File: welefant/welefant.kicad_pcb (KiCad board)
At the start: 2 copper layers, 80 x 90 mm, 72 parts, among them J1 Conn_02x11_Odd_Even, J2 Conn_02x11_Odd_Even, Q1 AO3400A, Q2 AO3401A, Q3 AO3401A, Q4 AO3400A, SW1 TS-1187A-B-A-B, SW2 TS-1187A-B-A-B, U1 ESP32-S3-WROOM-1-N8, U2 welefant, U3 XB8089D, U4 TP4056, U5 HE9073A33M5R, U6 MT3608L, U7 SK6812MINI-E_C5149201, U8 SK6812MINI-E_C5149201

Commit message: blubb
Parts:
- removed BUZZER1: MLT-8530, easyeda2kicad:BUZ-SMD_4P-L8.5-W8.5-P8.50-TL
- removed D5, D6, D7: SS34, easyeda2kicad:SMA_L4.3-W2.6-LS5.2-RD
- removed D8: BAV99,215, easyeda2kicad:SOT-23-3_L2.9-W1.6-P1.90-LS2.8-BR
- removed LED22, LED23, LED24, LED25: SK6812MINI-E, hacrafu:SK6812MINI-E-handsolder
- removed MIC1: ZTS6117, easyeda2kicad:MIC-SMD_4P-L2.8-W1.9-P1.84-TL_ZTS6117
- removed Q4: AO3400A, easyeda2kicad:SOT-23-3_L2.9-W1.6-P1.90-LS2.8-BR
- added ANT1: ANTENNA, hacrafu:antenna, F.Cu at (71.3, 36.8)
- added BT1: Battery, hacrafu:LiPo_Recycled_welefant, F.Cu at (59.4, 114.0)
- added C12: 10u, easyeda2kicad:C0603, F.Cu at (66.0, 50.7)
- added C13: 1u, easyeda2kicad:C0603, F.Cu at (67.6, 50.7)
- added C14: 1u, easyeda2kicad:C0603, F.Cu at (71.4, 49.9)
- added C15: 100n, easyeda2kicad:C0603, F.Cu at (69.3, 50.7)
- added C16: 100n, easyeda2kicad:C0603, F.Cu at (67.0, 55.8)
- added C17: 100n, easyeda2kicad:C0603, F.Cu at (73.5, 50.7)
- added C18: 4p7, easyeda2kicad:C0402, F.Cu at (76.0, 51.8)
- added C19: 3p3, easyeda2kicad:C0402, F.Cu at (76.0, 47.6)
- added C20: 100n, easyeda2kicad:C0603, F.Cu at (68.3, 70.3)
- added C21: 100n, easyeda2kicad:C0603, F.Cu at (77.8, 54.0)
- added C22: 1u, easyeda2kicad:C0603, F.Cu at (66.7, 70.3)
- added C23: 100n, easyeda2kicad:C0603, F.Cu at (79.2, 54.0)
- added C24: 100n, easyeda2kicad:C0603, F.Cu at (60.3, 59.5)
- added C25: 1u, easyeda2kicad:C0603, F.Cu at (87.3, 107.1)
- added C8: 10u, easyeda2kicad:C0603, F.Cu at (58.2, 71.0)
- added CLED1: yellow, easyeda2kicad:LED0603-RD-YELLOW, F.Cu at (48.5, 77.7)
- added D4: 1N5819WS, Diode_SMD:D_SOD-323, F.Cu at (48.1, 79.8)
- added J3: Conn_02x6_Odd_Even, hacrafu:PinHeader_2x06_P2.54mm_Vertical_SMD_handsolder, F.Cu at (92.0, 50.3)
- added L2: 2n2, easyeda2kicad:L0603, F.Cu at (75.4, 49.7)
- added LEDH_L1: SK6812MINI-E, hacrafu:SK6812MINI-E-handsolder, F.Cu at (80.0, 66.0)
- added LEDH_R1: SK6812MINI-E, hacrafu:SK6812MINI-E-handsolder, F.Cu at (63.2, 66.0)
- added R11: 10K, easyeda2kicad:R0603, F.Cu at (50.5, 88.1)
- added R12: 330, easyeda2kicad:R0603, F.Cu at (48.5, 76.1)
- added R13: 10K, easyeda2kicad:R0603, F.Cu at (48.9, 68.6)
- added R14: 1K, easyeda2kicad:R0603, F.Cu at (50.4, 68.6)
- added R15: 390K, easyeda2kicad:R0603, F.Cu at (56.5, 67.5)
- added R16: 100K, easyeda2kicad:R0603, F.Cu at (56.5, 69.4)
- added R17: 3K3, easyeda2kicad:R0603_NEW, F.Cu at (59.4, 76.2)
- added R18: 0, easyeda2kicad:R0603, F.Cu at (82.1, 59.3)
- added R19: 10K, easyeda2kicad:R0603, F.Cu at (44.2, 47.4)
- added R20: 330, easyeda2kicad:R0603, F.Cu at (66.8, 59.8)
- added R21: 0, easyeda2kicad:R0603, F.Cu at (75.3, 63.5)
- added R22: 0, easyeda2kicad:R0603, F.Cu at (74.0, 63.5)
- added R23: 0, easyeda2kicad:R0603, F.Cu at (72.5, 63.5)
- added R24: 0, easyeda2kicad:R0603, F.Cu at (71.2, 63.5)
- added R25: 0, easyeda2kicad:R0603, F.Cu at (69.8, 63.5)
- added SW3: BOOT, easyeda2kicad:SW-SMD_4P-L5.1-W5.1-P3.70-LS6.5-TL-2, F.Cu at (105.0, 45.5)
- added SW4: GPIO33, easyeda2kicad:SW-SMD_4P-L5.1-W5.1-P3.70-LS6.5-TL-2, F.Cu at (38.5, 52.5)
- added SW5: IO34, easyeda2kicad:SW-SMD_4P-L5.1-W5.1-P3.70-LS6.5-TL-2, F.Cu at (105.0, 52.5)
- added X1: 40 MHz, easyeda2kicad:OSC-SMD_4P-L3.2-W2.5-BL_SIT8008BI, F.Cu at (79.7, 59.0)
- C1: value 0.1u -> 33n; footprint easyeda2kicad:C0402_NEW -> easyeda2kicad:C0603
- C10: value 10u -> 15p
- C11: value 0.1u -> 15p; footprint easyeda2kicad:C0402_NEW -> easyeda2kicad:C0603
- C2: value 10u -> 33n
- C6: value 22u -> 1u; footprint easyeda2kicad:C0805 -> easyeda2kicad:C0603
- C7: value 22u -> 10u; footprint easyeda2kicad:C0805 -> easyeda2kicad:C0603
- C9: value 0.1u -> 10u; footprint easyeda2kicad:C0402_NEW -> easyeda2kicad:C0603
- D1: value 5V6 -> 3V3
- D3: value 3V3 -> 5V6
- J1: value Conn_02x11_Odd_Even -> Conn_01x02; footprint Connector_PinHeader_2.54mm:PinHeader_2x11_P2.54mm_Vertical_SMD -> Connector_JST:JST_PH_B2B-PH-K_1x02_P2.00mm_Vertical
- J2: value Conn_02x11_Odd_Even -> Conn_02x7_Odd_Even; footprint Connector_PinHeader_2.54mm:PinHeader_2x11_P2.54mm_Vertical_SMD -> hacrafu:PinHeader_2x07_P2.54mm_Vertical_SMD_handsolder
- L1: value 10u -> 2n2; footprint easyeda2kicad:IND-SMD_L8.0-W8.0 -> easyeda2kicad:L0603
- LED21: value SK6812MINI-E -> blue; footprint hacrafu:SK6812MINI-E-handsolder -> easyeda2kicad:LED0603-FD_BLUE
- Q1: value AO3400A -> AO3401A; footprint easyeda2kicad:SOT-23-3_L2.9-W1.6-P1.90-LS2.8-BR -> easyeda2kicad:SOT-23_L2.9-W1.3-P1.90-LS2.4-BR
- R1: value 5.1K -> 10K
- R10: value 10K -> 1K
- R2: value 1K -> 5.1K
- R3: value 5.1K -> 1K
- R4, R5: value 2.4K -> 270
- R6: value 10K -> 150
- R7: value 110K -> 150
- R8: value 110K -> 5.1K
- R9: value 15K -> 100K
- SW1: value TS-1187A-B-A-B -> ON-OFF; footprint easyeda2kicad:SW-SMD_4P-L5.1-W5.1-P3.70-LS6.5-TL-2 -> easyeda2kicad:SW-TH_K3-1296S-E1
- SW2: value TS-1187A-B-A-B -> RESET
- U1: value ESP32-S3-WROOM-1-N8 -> RT9080-33GJ5; footprint easyeda2kicad:WIFIM-SMD_ESP32-S3-WROOM-1-N8 -> easyeda2kicad:TSOT-23-5_L2.9-W1.6-P0.95-LS2.8-BL
- U2: value welefant -> Audio Jack PJ-324; footprint hacrafu:welefant -> easyeda2kicad:AUDIO-TH_PJ-32400
- U3: value XB8089D -> SD18OB261-060; footprint easyeda2kicad:SOIC-8_L5.0-W4.0-P1.27-LS6.0-BL-EP2.0 -> hacrafu:MIC-SMD_SD18OB261-060
- U5: value HE9073A33M5R -> welefant; footprint easyeda2kicad:SOT-23-5_L3.0-W1.7-P0.95-LS2.8-BL -> hacrafu:welefant; moved to B.Cu
- U6: value MT3608L -> 128MBit Flash; footprint easyeda2kicad:SOT-23-6_L2.9-W1.7-P0.95-LS2.8-BL -> easyeda2kicad:SOIC-8_L5.3-W5.3-P1.27-LS8.0-BL
- U7: value SK6812MINI-E_C5149201 -> ESP32-S3; footprint hacrafu:SK6812MINI-E-handsolder -> easyeda2kicad:QFN-56_L7.0-W7.0-P0.40-TL-EP4.0
- U8: value SK6812MINI-E_C5149201 -> Reset 2.8V; footprint hacrafu:SK6812MINI-E-handsolder -> easyeda2kicad:SOT-23-3_L2.9-W1.6-P1.90-LS2.8-BR
- moved J1 122.2 mm to (97.7, 103.2)
- moved LED13 115.2 mm to (87.2, 98.0), turned to 180 degrees
- moved LED17 107.7 mm to (87.2, 103.0), turned to 180 degrees
- moved LED15 105.3 mm to (67.2, 98.0), turned to 180 degrees
- moved LED16 104.6 mm to (57.2, 98.0), turned to 180 degrees
- moved LED14 102.7 mm to (77.2, 98.0), turned to 180 degrees
- moved LED18 101.7 mm to (77.2, 103.0), turned to 180 degrees
- moved SW1 96.5 mm to (42.8, 82.2), turned to 0 degrees
- moved U2 96.0 mm to (50.5, 111.2), turned to 6 degrees
- moved C5 94.2 mm to (46.2, 88.8), turned to -90 degrees
- moved LED9 93.8 mm to (87.2, 93.0), turned to 180 degrees
- moved LED19 92.5 mm to (67.2, 103.0), turned to 180 degrees
- moved LED11 92.1 mm to (67.2, 93.0), turned to 180 degrees
- moved LED10 89.0 mm to (77.2, 93.0), turned to 180 degrees
- moved LED2 88.9 mm to (77.2, 83.0), turned to 180 degrees
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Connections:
- C1 pad 1: Net-(C1-Pad1) -> GND
- C10 pad 1: Net-(BUZZER1-Pad1) -> /XTAL_N
- C10 pad 2: /GND -> GND
- C11 pad 1: Net-(R14-Pad2) -> GND
- C2 pad 1: /Power/VBAT -> GND
- C2 pad 2: /GND -> Net-(C2-Pad2)
- C3 pad 1: /Power/VUSB -> GND
- C3 pad 2: /GND -> /V33
- C4 pad 1: Net-(Q2-Pad2) -> Net-(C1-Pad2)
- C4 pad 2: /GND -> Net-(C4-Pad2)
- C5 pad 1: /GND -> Net-(C2-Pad2)
- C5 pad 2: /Power/V33 -> Net-(C5-Pad2)
- C6 pad 1: /Power/V5 -> GND
- C6 pad 2: /GND -> /VBUS
- C7 pad 1: Net-(C7-Pad1) -> /V5
- C7 pad 2: /GND -> GND
- C9 pad 1: /VEXT -> GND
- C9 pad 2: /GND -> /VBAT
- D1 pad 1: /Power/VUSB -> /USB_DP
- D1 pad 2: /GND -> GND
- D2 pad 1: /Power/USB_DP -> /USB_DN
- D2 pad 2: /GND -> GND
- D3 pad 1: /Power/USB_DN -> /V5
- D3 pad 2: /GND -> GND
- J1 pad 1: unconnected-(J1-Pad1) -> /VBAT
- J1 pad 2: unconnected-(J1-Pad2) -> GND
- J2 pad 1: unconnected-(J2-Pad1) -> GND
- J2 pad 10: unconnected-(J2-Pad10) -> /MIC_CLK
- J2 pad 11: unconnected-(J2-Pad11) -> /AUDIO_PWM_R
- J2 pad 12: unconnected-(J2-Pad12) -> /AUDIO_PWM_L
- J2 pad 13: unconnected-(J2-Pad13) -> /USB_DP
- J2 pad 14: unconnected-(J2-Pad14) -> /USB_DN
- J2 pad 2: unconnected-(J2-Pad2) -> /V33
- J2 pad 3: unconnected-(J2-Pad3) -> /RX
- J2 pad 4: unconnected-(J2-Pad4) -> /V5
- J2 pad 5: unconnected-(J2-Pad5) -> /TX
- J2 pad 6: unconnected-(J2-Pad6) -> /BAT_SENS
- J2 pad 7: unconnected-(J2-Pad7) -> /BAT_SENS_EN
- J2 pad 8: unconnected-(J2-Pad8) -> /MIC_DATA
- J2 pad 9: unconnected-(J2-Pad9) -> /JACK_SENS
- L1 pad 1: Net-(D7-Pad2) -> /V33
- L1 pad 2: Net-(C7-Pad1) -> Net-(C17-Pad2)
- LED1 pad 1: /LEDs/VUSB -> /VEXT
- LED1 pad 2: unconnected-(LED1-Pad2) -> Net-(LED1-DOUT)
- LED1 pad 3: /LEDs/GND -> GND
- LED1 pad 4: Net-(LED1-Pad4) -> /LED_MATRIX
- LED10 pad 1: /LEDs/VUSB -> /VEXT
- LED10 pad 2: Net-(LED10-Pad2) -> Net-(LED10-DOUT)
- LED10 pad 3: /LEDs/GND -> GND
- LED10 pad 4: unconnected-(LED10-Pad4) -> Net-(LED10-DIN)
- LED11 pad 1: /LEDs/VUSB -> /VEXT
- LED11 pad 2: unconnected-(LED11-Pad2) -> Net-(LED11-DOUT)
- LED11 pad 3: /LEDs/GND -> GND
- LED11 pad 4: Net-(LED11-Pad4) -> Net-(LED10-DOUT)
- LED12 pad 1: /LEDs/VUSB -> /VEXT
- LED12 pad 2: Net-(LED11-Pad4) -> /D3_LED
- LED12 pad 3: /LEDs/GND -> GND
- LED12 pad 4: Net-(LED12-Pad4) -> Net-(LED11-DOUT)
- LED13 pad 1: /LEDs/VUSB -> /VEXT
- LED13 pad 2: Net-(LED12-Pad4) -> Net-(LED13-DOUT)
- LED13 pad 3: /LEDs/GND -> GND
- LED13 pad 4: Net-(LED13-Pad4) -> /D3_LED
- LED14 pad 1: /LEDs/VUSB -> /VEXT
- LED14 pad 2: Net-(LED13-Pad4) -> Net-(LED14-DOUT)
- LED14 pad 3: /LEDs/GND -> GND
- LED14 pad 4: Net-(LED14-Pad4) -> Net-(LED13-DOUT)
- LED15 pad 1: /LEDs/VUSB -> /VEXT
- LED15 pad 2: Net-(LED14-Pad4) -> Net-(LED15-DOUT)
- LED15 pad 3: /LEDs/GND -> GND
- LED15 pad 4: unconnected-(LED15-Pad4) -> Net-(LED14-DOUT)
- LED16 pad 1: /LEDs/VUSB -> /VEXT
- LED16 pad 2: unconnected-(LED16-Pad2) -> /D4_LED
- LED16 pad 3: /LEDs/GND -> GND
- LED16 pad 4: Net-(LED16-Pad4) -> Net-(LED15-DOUT)
- LED17 pad 1: /LEDs/VUSB -> /VEXT
- LED17 pad 2: Net-(LED16-Pad4) -> Net-(LED17-DOUT)
- LED17 pad 3: /LEDs/GND -> GND
- LED17 pad 4: Net-(LED17-Pad4) -> /D4_LED
- LED18 pad 1: /LEDs/VUSB -> /VEXT
- LED18 pad 2: Net-(LED17-Pad4) -> Net-(LED18-DOUT)
- LED18 pad 3: /LEDs/GND -> GND
- LED18 pad 4: Net-(LED18-Pad4) -> Net-(LED17-DOUT)
- LED19 pad 1: /LEDs/VUSB -> /VEXT
- LED19 pad 2: Net-(LED18-Pad4) -> Net-(LED19-DOUT)
- LED19 pad 3: /LEDs/GND -> GND
- LED19 pad 4: Net-(LED19-Pad4) -> Net-(LED18-DOUT)
- LED2 pad 1: /LEDs/VUSB -> /VEXT
- LED2 pad 2: Net-(LED1-Pad4) -> Net-(LED2-DOUT)
- LED2 pad 3: /LEDs/GND -> GND
- LED2 pad 4: Net-(LED2-Pad4) -> Net-(LED1-DOUT)
- LED20 pad 1: /LEDs/VUSB -> /VEXT
- LED20 pad 2: Net-(LED19-Pad4) -> unconnected-(LED20-DOUT-Pad2)
- LED20 pad 3: /LEDs/GND -> GND
- LED20 pad 4: unconnected-(LED20-Pad4) -> Net-(LED19-DOUT)
- LED21 pad 1: /LEDs/VUSB -> Net-(LED21-C)
- LED21 pad 2: unconnected-(LED21-Pad2) -> /LED
- LED3 pad 1: /LEDs/VUSB -> /VEXT
- LED3 pad 2: Net-(LED2-Pad4) -> Net-(LED3-DOUT)
- LED3 pad 3: /LEDs/GND -> GND
- LED3 pad 4: Net-(LED3-Pad4) -> Net-(LED2-DOUT)
- LED4 pad 1: /LEDs/VUSB -> /VEXT
- LED4 pad 2: Net-(LED3-Pad4) -> /D1_LED
- LED4 pad 3: /LEDs/GND -> GND
- LED4 pad 4: Net-(LED4-Pad4) -> Net-(LED3-DOUT)
- LED5 pad 1: /LEDs/VUSB -> /VEXT
- LED5 pad 2: Net-(LED4-Pad4) -> Net-(LED5-DOUT)
- LED5 pad 3: /LEDs/GND -> GND
- LED5 pad 4: unconnected-(LED5-Pad4) -> /D1_LED
- LED6 pad 1: /LEDs/VUSB -> /VEXT
- LED6 pad 2: unconnected-(LED6-Pad2) -> Net-(LED6-DOUT)
- LED6 pad 3: /LEDs/GND -> GND
- LED6 pad 4: Net-(LED6-Pad4) -> Net-(LED5-DOUT)
- LED7 pad 1: /LEDs/VUSB -> /VEXT
- LED7 pad 2: Net-(LED6-Pad4) -> Net-(LED7-DOUT)
- LED7 pad 3: /LEDs/GND -> GND
- LED7 pad 4: Net-(LED7-Pad4) -> Net-(LED6-DOUT)
- LED8 pad 1: /LEDs/VUSB -> /VEXT
- LED8 pad 2: Net-(LED7-Pad4) -> /D2_LED
- LED8 pad 3: /LEDs/GND -> GND
- LED8 pad 4: Net-(LED8-Pad4) -> Net-(LED7-DOUT)
- LED9 pad 1: /LEDs/VUSB -> /VEXT
- LED9 pad 2: Net-(LED8-Pad4) -> Net-(LED10-DIN)
- LED9 pad 3: /LEDs/GND -> GND
- LED9 pad 4: Net-(LED10-Pad2) -> /D2_LED
- Q1 pad 1: /VEXT_EN -> Net-(Q1-G)
- Q1 pad 2: /Power/V33 -> /V33
- Q2 pad 1: /Power/VUSB -> Net-(Q2-G)
- Q2 pad 2: Net-(Q2-Pad2) -> Net-(D4-K)
- Q2 pad 3: /Power/VBAT -> /VBAT
- Q3 pad 1: /Power/VUSB -> Net-(Q3-G)
- Q3 pad 2: Net-(C7-Pad1) -> /VBAT
- Q3 pad 3: /Power/VBAT -> Net-(Q3-D)
- R1 pad 1: /GND -> /V33
- R1 pad 2: Net-(R1-Pad2) -> /VEXT_EN
- R10 pad 1: /GND -> Net-(Q2-G)
- R10 pad 2: /Power/VUSB -> /V5
- R2 pad 1: /Power/VBAT -> GND
- R2 pad 2: Net-(C1-Pad2) -> Net-(USB1-CC2)
- R3 pad 1: Net-(R3-Pad1) -> Net-(Q1-G)
- R3 pad 2: /GND -> /VEXT_EN
- R4 pad 1: Net-(D4-Pad1) -> /AUDIO_PWM_L
- R4 pad 2: Net-(R4-Pad2) -> Net-(C1-Pad2)
- R5 pad 1: Net-(R5-Pad1) -> /AUDIO_PWM_R
- R5 pad 2: /GND -> Net-(C2-Pad2)
- R6 pad 1: /Power/VUSB -> GND
- R6 pad 2: /GND -> Net-(C1-Pad2)
- R7 pad 1: Net-(R7-Pad1) -> GND
- R7 pad 2: /Power/V5 -> Net-(C2-Pad2)
- R8 pad 1: Net-(R8-Pad1) -> Net-(USB1-CC1)
- R8 pad 2: /GND -> GND
- R9 pad 1: /GND -> Net-(U1-EN)
- R9 pad 2: Net-(R7-Pad1) -> /VBUS
- SW1 pad 1: /EN -> unconnected-(SW1-Pad1)
- SW1 pad 2: unconnected-(SW1-Pad2) -> Net-(D4-K)
- SW1 pad 3: /GND -> /VBUS
- SW2 pad 1: /IO0 -> /RESET
- SW2 pad 2: unconnected-(SW2-Pad2) -> /RESET
- SW2 pad 3: /GND -> GND
- SW2 pad 4: unconnected-(SW2-Pad4) -> GND
- U1 pad 1: /GND -> /VBUS
- U1 pad 2: /Power/V33 -> GND
- U1 pad 3: /EN -> Net-(U1-EN)
- U1 pad 5: unconnected-(U1-Pad5) -> /V33
- U2 pad 1: unconnected-(U2-Pad1) -> GND
- U2 pad 2: unconnected-(U2-Pad2) -> Net-(C5-Pad2)
- U2 pad 3: unconnected-(U2-Pad3) -> /JACK_SENS
- U2 pad 5: unconnected-(U2-Pad5) -> Net-(C4-Pad2)
- U3 pad 1: /GND -> /MIC_DATA
- U3 pad 2: /GND -> GND
- U3 pad 3: /GND -> GND
- U3 pad 4: /GND -> /MIC_CLK
- U3 pad 5: Net-(C1-Pad1) -> /VEXT
- U4 pad 1: /GND -> GND
- U4 pad 2: Net-(R5-Pad1) -> Net-(U4-PROG)
- U4 pad 3: /GND -> GND
- U4 pad 4: /Power/VUSB -> /V5
- U4 pad 5: /Power/VBAT -> /VBAT
- U4 pad 7: Net-(R4-Pad2) -> Net-(U4-~{CHRG})
- U4 pad 8: /Power/VUSB -> /V5
- U4 pad 9: unconnected-(U4-Pad9) -> GND
- U5 pad 1: Net-(Q2-Pad2) -> /TOUCH_EL
- U5 pad 2: /GND -> /TOUCH_ER
- U5 pad 3: Net-(Q2-Pad2) -> /TOUCH_T1
- U5 pad 4: unconnected-(U5-Pad4) -> /TOUCH_T2
- U5 pad 5: /Power/V33 -> /TOUCH_T3
- U6 pad 1: Net-(D7-Pad2) -> /SPICS0
- U6 pad 2: /GND -> /SPIQ
- U6 pad 3: Net-(R7-Pad1) -> /SPIWP
- U6 pad 4: /Power/V5_EN -> GND
- U6 pad 5: Net-(C7-Pad1) -> /SPID
- U6 pad 6: Net-(R8-Pad1) -> /SPICLK
- U7 pad 1: /LEDs/VUSB -> Net-(U7-LNA_IN)
- U7 pad 2: unconnected-(U7-Pad2) -> Net-(C17-Pad2)
- U7 pad 3: /LEDs/GND -> Net-(C17-Pad2)
- U7 pad 4: Net-(U7-Pad4) -> /RESET
- U8 pad 1: /LEDs/VUSB -> /RESET
- U8 pad 2: Net-(U7-Pad4) -> GND
- U8 pad 3: /LEDs/GND -> /V33
- USB1 pad 1: (no net) -> unconnected-(USB1-SH-Pad1)
- USB1 pad A1: /GND -> GND
- USB1 pad A12: /GND -> GND
- USB1 pad A4: /Power/VUSB -> /V5
- USB1 pad A5: Net-(R3-Pad1) -> Net-(USB1-CC1)
- USB1 pad A6: /Power/USB_DP -> /USB_DP
- USB1 pad A7: /Power/USB_DN -> /USB_DN
- USB1 pad A9: /Power/VUSB -> /V5
- USB1 pad B1: /GND -> GND
- USB1 pad B12: /GND -> GND
- USB1 pad B4: /Power/VUSB -> /V5
- USB1 pad B5: Net-(R1-Pad2) -> Net-(USB1-CC2)
- USB1 pad B6: /Power/USB_DP -> /USB_DP
- USB1 pad B7: /Power/USB_DN -> /USB_DN
- USB1 pad B9: /Power/VUSB -> /V5
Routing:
- net /VEXT: track 0.00 -> 275.1 mm, vias 0 -> 15
- net /TOUCH_T1: track 0.00 -> 127.9 mm, vias 0 -> 3
- net /TOUCH_T2: track 0.00 -> 121.3 mm, vias 0 -> 3
- net /V33: track 0.00 -> 113.3 mm, vias 0 -> 9
- net /VBAT: track 0.00 -> 110.6 mm, vias 0 -> 6
- net /TOUCH_T3: track 0.00 -> 110.3 mm, vias 0 -> 3
- net GND: track 0.00 -> 101.2 mm, vias 0 -> 458
- net /JACK_SENS: track 0.00 -> 89.6 mm, vias 0 -> 2
- net /TOUCH_T6: track 0.00 -> 88.5 mm, vias 0 -> 3
- net /TOUCH_T4: track 0.00 -> 88.2 mm, vias 0 -> 3
- net /TOUCH_T5: track 0.00 -> 83.2 mm, vias 0 -> 3
- net /V5: track 0.00 -> 76.0 mm, vias 0 -> 4
- net /USB_DP: track 0.00 -> 74.6 mm, vias 0 -> 2
- net /VEXT_EN: track 0.00 -> 70.0 mm, vias 0 -> 6
- net /USB_DN: track 0.00 -> 66.4 mm
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- added copper zone on B.Cu, net GND
- added copper zone on F.Cu, net GND
- removed copper zone on B.Cu, net /GND
- removed copper zone on F.Cu, net /GND
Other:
- outline, holes or cut-outs redrawn
- board text added: "3V3"
- board text added: "AL"
- board text added: "AR"
- board text added: "BAT SE"
- board text added: "BAT SENS"
- board text added: "GND"
- board text added: "IO33"
- board text added: "IO34"
- board text added: "IO35"
- board text added: "IO36"
- board text added: "IO37"
- board text added: "IO38"
- board text added: "IO39"
- board text added: "IO40"
- board text added: "IO41"
- board text added: "IO42"
- board text added: "JACK SENS"
- board text added: "JLCJLCJLCJLC"
- board text added: "MIC C"
- board text added: "MIC DATA"
- board text added: "OFF"
- board text added: "ON"
- board text added: "RX"
- board text added: "TX"
- board text added: "U+"
- board text added: "U-"
- board text added: "V5 USB"
- board text added: "VEXT"
- board text added: "VEXT EN"
- board text added: "Welefant ${ISSUE_DATE} CC-BY-NC-SA 4.0 HaCraFu e.V. Martin Müllenhaupt https://hacrafu.de/kits"

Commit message: welefant bestellung
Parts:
- removed J1: Conn_01x02, Connector_JST:JST_PH_B2B-PH-K_1x02_P2.00mm_Vertical
- added BT2: Conn_01x02, Connector_JST:JST_XH_B2B-XH-A_1x02_P2.50mm_Vertical, F.Cu at (95.7, 102.1)

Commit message: stand
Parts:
- removed C20: 100n, easyeda2kicad:C0603
- removed C22: 1u, easyeda2kicad:C0603
- removed R21, R22, R23, R24, R25: 0, easyeda2kicad:R0603
- removed U6: 128MBit Flash, easyeda2kicad:SOIC-8_L5.3-W5.3-P1.27-LS8.0-BL
- C17: footprint easyeda2kicad:C0603 -> easyeda2kicad:C0402_NEW
- C18: value 4p7 -> 3p3; footprint easyeda2kicad:C0402 -> easyeda2kicad:C0603
- C19: footprint easyeda2kicad:C0402 -> easyeda2kicad:C0603
- J2: value Conn_02x7_Odd_Even -> Conn_02x6_Odd_Even; footprint hacrafu:PinHeader_2x07_P2.54mm_Vertical_SMD_handsolder -> hacrafu:PinHeader_2x06_P2.54mm_Vertical_SMD_handsolder
- J3: value Conn_02x6_Odd_Even -> Conn_02x7_Odd_Even; footprint hacrafu:PinHeader_2x06_P2.54mm_Vertical_SMD_handsolder -> hacrafu:PinHeader_2x07_P2.54mm_Vertical_SMD_handsolder
- U7: value ESP32-S3 -> ESP32-S3(FN8)
- moved C14 28.2 mm to (44.0, 43.2), turned to 90 degrees
- moved C18 9.74 mm to (77.4, 42.2)
- moved C12 6.22 mm to (66.4, 44.5)
- moved C15 6.20 mm to (69.8, 44.5)
- moved L1 6.20 mm to (72.1, 45.2)
- moved C13 6.19 mm to (68.1, 44.5)
- moved C17 5.75 mm to (74.2, 45.0)
- moved C23 5.49 mm to (81.3, 48.9)
- moved U7 5.44 mm to (74.1, 52.0)
- moved C21 5.39 mm to (79.6, 48.9)
- moved L2 5.36 mm to (76.7, 44.5)
- moved R20 5.13 mm to (65.0, 54.9)
- moved R18 4.87 mm to (83.0, 54.5)
- moved C10 4.77 mm to (79.9, 51.4)
- moved X1 4.63 mm to (80.5, 54.5)
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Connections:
- C18 pad 2: Net-(U7-LNA_IN) -> Net-(ANT1-FEED)
- C19 pad 2: Net-(ANT1-PadFEED) -> Net-(U7-LNA_IN)
- J2 pad 10: /MIC_CLK -> /AUDIO_PWM_L
- J2 pad 11: /AUDIO_PWM_R -> /USB_DP
- J2 pad 12: /AUDIO_PWM_L -> /USB_DN
- J2 pad 3: /RX -> /V5
- J2 pad 4: /V5 -> /BAT_SENS
- J2 pad 5: /TX -> /BAT_SENS_EN
- J2 pad 6: /BAT_SENS -> /MIC_CLK
- J2 pad 7: /BAT_SENS_EN -> /JACK_SENS
- J2 pad 9: /JACK_SENS -> /AUDIO_PWM_R
- J3 pad 10: /IO40 -> /IO38
- J3 pad 11: /IO41 -> /IO39
- J3 pad 12: /IO42 -> /IO40
- J3 pad 5: /IO35 -> /RX
- J3 pad 6: /IO36 -> /TX
- J3 pad 7: /IO37 -> /IO35
- J3 pad 8: /IO38 -> /IO36
- J3 pad 9: /IO39 -> /IO37
- L2 pad 2: Net-(ANT1-PadFEED) -> Net-(ANT1-FEED)
- U7 pad 29: /VDD_SPI -> unconnected-(U7-VDD_SPI-Pad29)
- U7 pad 30: Net-(U7-SPIHD) -> unconnected-(U7-SPIHD-Pad30)
- U7 pad 31: Net-(U7-SPIWP) -> unconnected-(U7-SPIWP-Pad31)
- U7 pad 32: /SPICS0 -> unconnected-(U7-SPICS0-Pad32)
- U7 pad 33: Net-(U7-SPICLK) -> unconnected-(U7-SPICLK-Pad33)
- U7 pad 34: Net-(U7-SPIQ) -> unconnected-(U7-SPIQ-Pad34)
- U7 pad 35: Net-(U7-SPID) -> unconnected-(U7-SPID-Pad35)
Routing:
- net /TX: track 30.8 -> 12.4 mm
- net /VDD_SPI: track 15.6 -> 0.00 mm
- net /SPIQ: track 14.6 -> 0.00 mm
- net /SPICS0: track 13.8 -> 0.00 mm, vias 2 -> 0
- net /RX: track 31.2 -> 19.8 mm
- net /TOUCH_EL: track 37.9 -> 27.4 mm
- net /SPIWP: track 10.2 -> 0.00 mm
- net Net-(ANT1-PadFEED): track 8.97 -> 0.00 mm
- net /USB_DP: track 74.6 -> 83.0 mm
- net /USB_DN: track 66.4 -> 74.7 mm
- net /V33: track 113.3 -> 121.3 mm, vias 9 -> 8
- net GND: track 101.2 -> 93.9 mm, vias 458 -> 281
- net /VEXT_EN: track 70.0 -> 77.1 mm, vias 6 -> 4
- net /BAT_SENS: track 35.9 -> 42.0 mm
- net /SPID: track 5.68 -> 0.00 mm
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
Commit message: welefant redesign
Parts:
- D1, D2: value 3V3 -> 5V6; footprint easyeda2kicad:LL-34_L3.5-W1.5-RD -> easyeda2kicad:SOD-523_L1.2-W0.8-LS1.6-BI
- D3: footprint easyeda2kicad:LL-34_L3.5-W1.5-RD -> easyeda2kicad:SOD-523_L1.2-W0.8-LS1.6-BI
- LED21: value blue -> white; footprint easyeda2kicad:LED0603-FD_BLUE -> easyeda2kicad:LED0603-R-RD_WHITE
- moved D1 1.71 mm to (62.7, 69.9)
- moved D2 1.00 mm to (64.1, 69.9)
- moved D3 0.87 mm to (50.4, 89.9)
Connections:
- LED21 pad 1: Net-(LED21-C) -> /LED
- LED21 pad 2: /LED -> Net-(LED21-K)
- R20 pad 2: Net-(LED21-C) -> Net-(LED21-K)
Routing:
- net /USB_DN: track 74.7 -> 76.4 mm
- net Net-(LED21-K): track 0.00 -> 1.60 mm
- net Net-(LED21-C): track 1.60 -> 0.00 mm
- net /USB_DP: track 83.0 -> 82.2 mm
- net /V33: track 121.3 -> 121.9 mm
- net GND: vias 281 -> 308

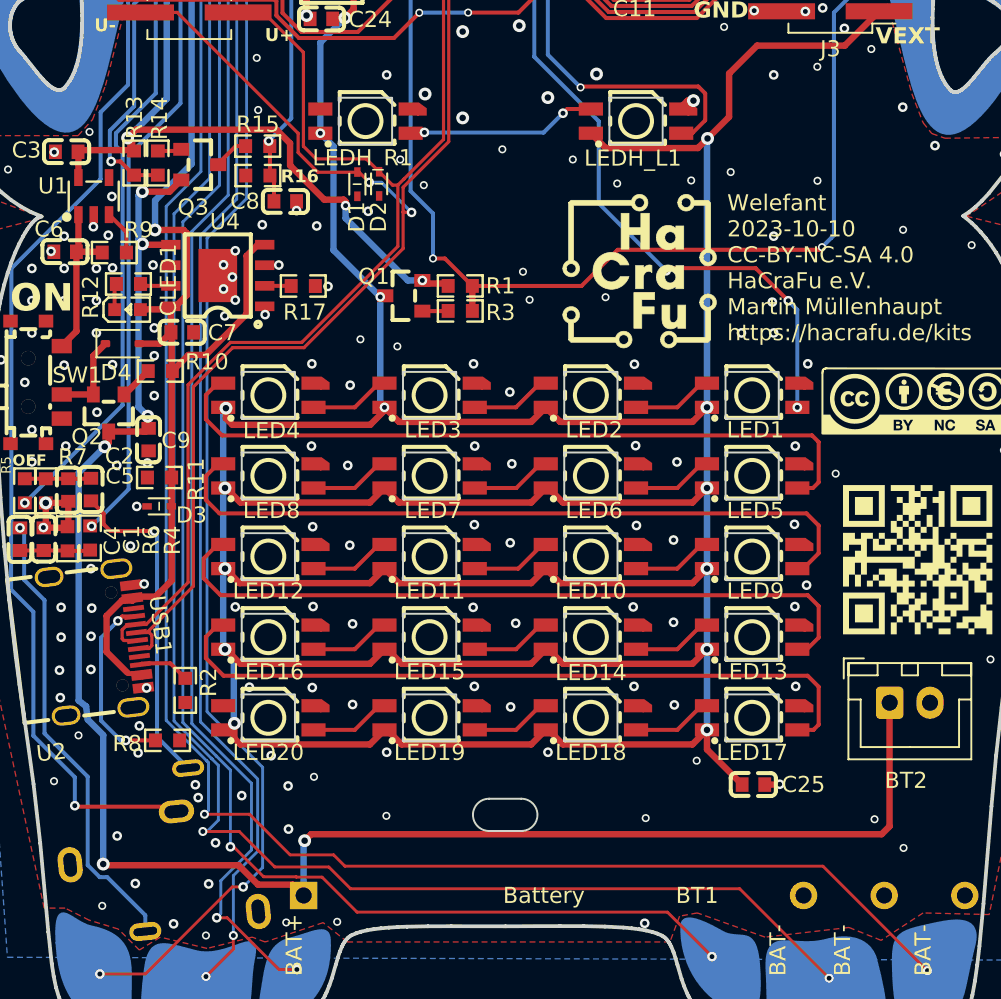
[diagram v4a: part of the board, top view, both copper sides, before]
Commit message: welefant: add fuse and make LED cutout smaller
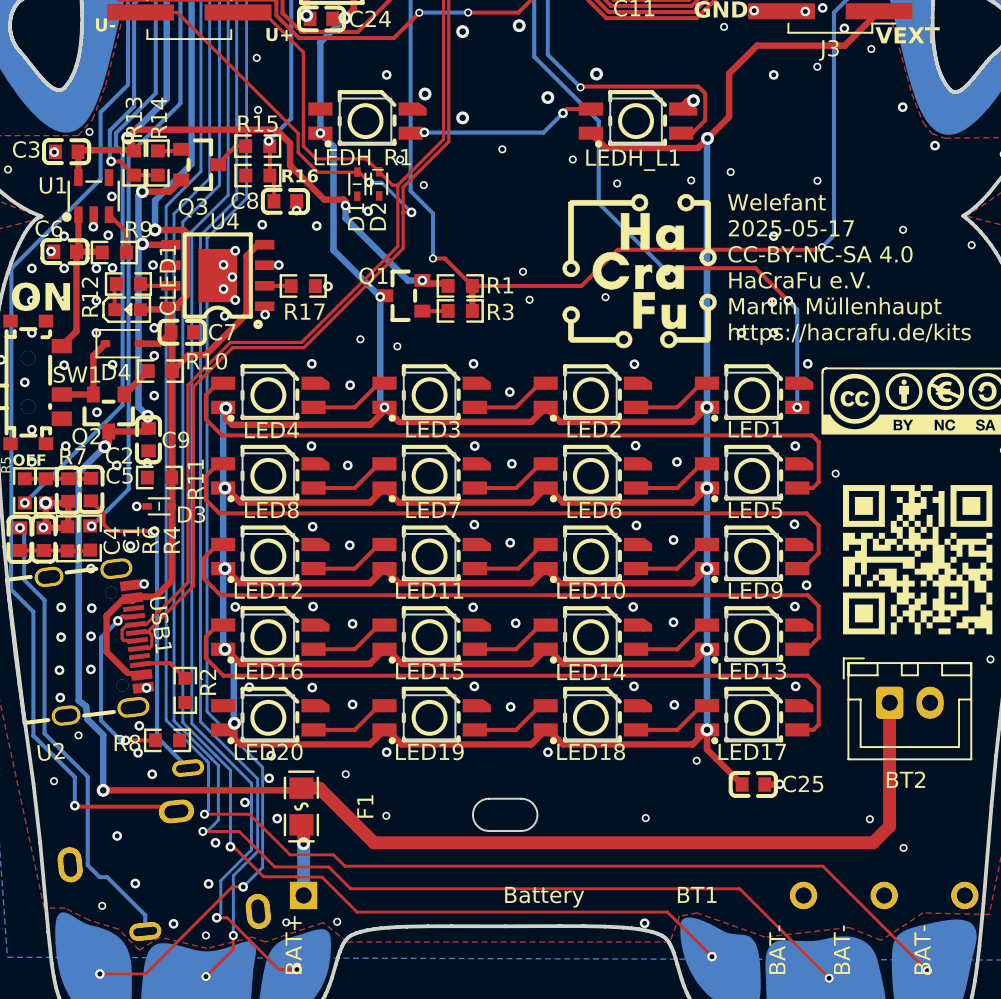
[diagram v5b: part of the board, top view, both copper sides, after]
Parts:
- added F1: Fuse, easyeda2kicad:F0805, F.Cu at (59.2, 108.5)
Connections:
- BT1 pad 1: /VBAT -> Net-(BT1-+)
- C9 pad 2: /VBAT -> Net-(BT1-+)
- D4 pad 1: Net-(D4-K) -> /VBAT
- Q2 pad 2: Net-(D4-K) -> /VBAT
- SW1 pad 2: Net-(D4-K) -> /VBAT
- U4 pad 5: /VBAT -> Net-(BT1-+)
- USB1 pad 1: unconnected-(USB1-SH-Pad1) -> (no net)
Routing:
- net Net-(D4-K): track 5.43 -> 0.00 mm
- net Net-(BT1-+): track 0.00 -> 4.43 mm, vias 0 -> 1
- net /VBAT: track 110.8 -> 109.0 mm, vias 6 -> 5
- net GND: vias 308 -> 307

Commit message: stand bestellung 18.5.25
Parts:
- removed C14: 1u, easyeda2kicad:C0603
- removed R19: 10K, easyeda2kicad:R0603
- removed U8: Reset 2.8V, easyeda2kicad:SOT-23-3_L2.9-W1.6-P1.90-LS2.8-BR
- added U6: Reset 2V9, easyeda2kicad:SOT-143_L2.9-W1.3-P1.92-LS2.3-BR, F.Cu at (44.7, 45.9)
- CLED1: footprint easyeda2kicad:LED0603-RD-YELLOW -> easyeda2kicad:LED0805-R-RD
- D1, D2, D3: footprint easyeda2kicad:SOD-523_L1.2-W0.8-LS1.6-BI -> easyeda2kicad:SOD-882_L1.0-W0.6-BI
- moved D1 3.57 mm to (65.9, 71.5), turned to 0 degrees
- moved D2 1.04 mm to (64.9, 70.6), turned to 180 degrees
- moved D3 0.34 mm to (50.6, 89.6)
- moved R12 0.32 mm to (48.5, 75.8)
- moved CLED1 0.29 mm to (48.2, 77.7)
- turned SW2 to 0 degrees
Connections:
- BT2 pad 1: /VBAT -> Net-(BT1-+)
- C9 pad 2: Net-(BT1-+) -> /VBAT
- CLED1 pad 1: Net-(CLED1-C) -> /V5
- CLED1 pad 2: /V5 -> Net-(CLED1--)
- D4 pad 1: /VBAT -> Net-(D4-K)
- J2 pad 11: /USB_DP -> /GPIO33
- J2 pad 12: /USB_DN -> /VBAT
- Q2 pad 2: /VBAT -> Net-(D4-K)
- R12 pad 1: Net-(CLED1-C) -> Net-(CLED1--)
- SW1 pad 2: /VBAT -> Net-(D4-K)
- U4 pad 5: Net-(BT1-+) -> /VBAT
- U7 pad 4: /RESET -> Net-(U6-~{RESET})
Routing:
- net Net-(BT1-+): track 4.43 -> 49.5 mm
- net /RESET: track 51.3 -> 9.03 mm
- net /VBAT: track 109.0 -> 72.0 mm, vias 5 -> 6
- net Net-(U6-~{RESET}): track 0.00 -> 32.8 mm
- net /USB_DP: track 82.2 -> 58.7 mm, vias 2 -> 0
- net /USB_DN: track 76.4 -> 58.6 mm
- net GND: track 93.9 -> 85.7 mm, vias 307 -> 306
- net Net-(D4-K): track 0.00 -> 5.43 mm
- net Net-(CLED1--): track 0.00 -> 2.18 mm
- net Net-(CLED1-C): track 1.62 -> 0.00 mm
- net /V33: track 121.9 -> 120.6 mm
- net /D2_LED: track 45.0 -> 45.9 mm
- net /GPIO33: track 48.8 -> 49.7 mm
- net /D4_LED: track 45.2 -> 46.1 mm
- net /D3_LED: track 45.2 -> 46.1 mm
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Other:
- board text added: "VBAT"
- board text removed: "U+"
- board text removed: "U-"
